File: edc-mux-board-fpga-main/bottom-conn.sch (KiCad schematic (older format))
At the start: 1 part

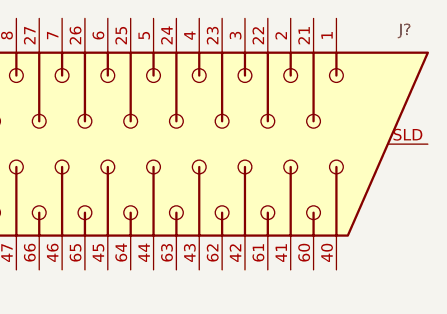
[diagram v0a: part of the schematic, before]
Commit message: finishing ethernet modifications, annotating and finishing footprint assignment
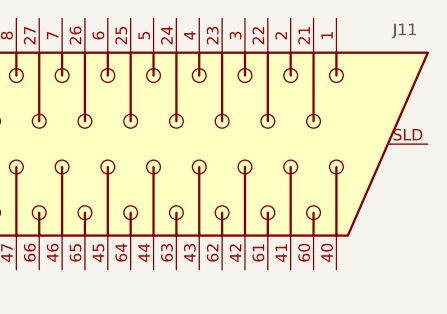
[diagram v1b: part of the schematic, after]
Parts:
- J11: renamed from J?; footprint (none) -> SW-Harting:09565525612; Description (none) -> DD-78 female right angle connector Through hole; Manufacturer (none) -> Harting; Manufacturers Part Number (none) -> 09565525612; Package ID (none) -> Through Hole
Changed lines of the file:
@@
 $Descr USLedger 17000 11000
 encoding utf-8
-Sheet 27 19
+Sheet 18 19
 Title "EDC Mux Board"
 Date "2019-05-17"
@@
 $EndDescr
 $Comp
-L SW-con:DD-78F J?
+L SW-con:DD-78F J11
 U 1 1 5D6FD788
 P 8100 5950
-F 0 "J?" H 10400 6450 50  0000 C CNN
+F 0 "J11" H 10400 6450 50  0000 C CNN
 F 1 "DD-78F" H 6000 6450 50  0000 C CNN
-F 2 "" H 8200 5500 50  0001 C CNN
-F 3 "" H 8800 5550 50  0001 C CNN
+F 2 "SW-Harting:09565525612" H 8200 5500 50  0001 C CNN
+F 3 "https://b2b.harting.com/files/download/PRD/PDF_TS/0956552X612_100510349DRW001B.pdf" H 8800 5550 50  0001 C CNN
+F 4 "Through Hole" H 0   0   50  0001 C CNN "Package ID"
+F 5 "DD-78 female right angle connector Through hole" H 0   0   50  0001 C CNN "Description"
+F 6 "Harting" H 0   0   50  0001 C CNN "Manufacturer"
+F 7 "09565525612" H 0   0   50  0001 C CNN "Manufacturers Part Number"
 	1    8100 5950
 	1    0    0    -1

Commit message: copying bottom conn from expansion to main
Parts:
- removed J11: DD-78F, SW-Harting:09565525612, symbol SW-con:DD-78F
- added J11: DC-62F, SW-Harting:09564525612, symbol SW-con:DC-62F
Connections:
- net labels added: +12V, BCLK10, BCLK11, BCLK12, BCLK13, BCLK14, BCLK15, BCLK8, BCLK9, DIN10, DIN11, DIN12, DIN13, DIN14, DIN15, DIN8, DIN9, DOUT10, DOUT11, DOUT12, DOUT13, DOUT14, DOUT15, DOUT8, DOUT9, GND, ID_PIN10, ID_PIN11, ID_PIN12, ID_PIN13, ID_PIN14, ID_PIN15, ID_PIN8, ID_PIN9, INT_10, INT_11, INT_12, INT_13, INT_14, INT_15, INT_8, INT_9, WCLK10, WCLK11, WCLK12, WCLK13, WCLK14, WCLK15, WCLK8, WCLK9
- wire segments 0 -> 78

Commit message: Reannotate main schematic and pcb after expansion transition
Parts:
- renumbered J11 to J14
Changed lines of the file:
@@
 INT_[8..15]
 $Comp
-L power:+12V #PWR090
+L power:+12V #PWR0159
 U 1 1 5D5500B2
 P 8450 4550
-F 0 "#PWR090" H 8450 4400 50  0001 C CNN
+F 0 "#PWR0159" H 8450 4400 50  0001 C CNN
 F 1 "+12V" H 8450 4690 50  0000 C CNN
 F 2 "" H 8450 4550 50  0001 C CNN
@@
 $EndComp
 $Comp
-L power:GND #PWR091
+L power:GND #PWR0160
 U 1 1 5D550BF6
 P 8500 7400
-F 0 "#PWR091" H 8500 7150 50  0001 C CNN
+F 0 "#PWR0160" H 8500 7150 50  0001 C CNN
 F 1 "GND" H 8500 7250 50  0000 C CNN
 F 2 "" H 8500 7400 50  0001 C CNN
@@
 CLK2_CODEC
 $Comp
-L power:GND #PWR0108
+L power:GND #PWR0161
 U 1 1 5D3521DF
 P 11050 6900
-F 0 "#PWR0108" H 11050 6650 50  0001 C CNN
+F 0 "#PWR0161" H 11050 6650 50  0001 C CNN
 F 1 "GND" H 11050 6750 50  0000 C CNN
 F 2 "" H 11050 6900 50  0001 C CNN
@@
 	11050 6700 11050 6900
 $Comp
-L SW-con:DC-62F J11
+L SW-con:DC-62F J14
 U 1 1 5D2FFC98
 P 8500 6700
-F 0 "J11" H 10700 7050 50  0000 C CNN
+F 0 "J14" H 10700 7050 50  0000 C CNN
 F 1 "DC-62F" H 6100 7000 50  0000 C CNN
 F 2 "SW-Harting:09564525612" H 8500 6100 50  0001 C CNN

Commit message: s/Manufacturers Part Number/MPN/g
for compatability with MacroFab automated processing
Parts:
- J14: MPN (none) -> 09564525612; Manufacturers Part Number 09564525612 -> (none)
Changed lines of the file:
@@
 F 4 "DC-62 Connector" H 0   0   50  0001 C CNN "Description"
 F 5 "Harting" H 0   0   50  0001 C CNN "Manufacturer"
-F 6 "09564525612" H 0   0   50  0001 C CNN "Manufacturers Part Number"
+F 6 "09564525612" H 0   0   50  0001 C CNN "MPN"
 F 7 "Through Hole" H 0   0   50  0001 C CNN "Package ID"
 	1    8500 6700
